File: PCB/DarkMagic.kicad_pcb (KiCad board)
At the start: 6 copper layers, 157 x 73 mm, 212 parts, among them IC1 5PB1106PGGI8, IC10 MMBT3904-AQ, IC11 MMBT3904-AQ, IC12 SN74LVC1G125DBVT, IC13 SN74LVC1G125DBVT, IC14 LM3940IMP-3.3_NOPB, IC15 SN74LVC1G125DBVT, IC17 LM393DR, IC2 ESP32-WROOM-32UE-N16, IC3 MMBT3904-AQ, IC4 MMBT3904-AQ, IC5 W5500, IC6 CP2102N-A02-GQFN24, IC7 USBLC6-2SC6, IC8 LMR33640ADDAR, J1 USB_C_Receptacle_USB2.0_16P, J2 TMJ0026ABNL, J3 5747842-2, J4 Screw_Terminal_01x02, J5 Screw_Terminal_01x02, J6 5747842-2, J7 171825-2, J9 Conn_01x04, Q1 SQ2319ADS-T1_BE3, Q2 SQ2348ES-T1_BE3, U1 SC16IS752IPW_128, U2 SC16IS752IPW_128, U3 CD74HC138QM96Q1, U4 SC16IS752IPW_128, U5 SC16IS752IPW_128, U6 SC16IS752IPW_128, U7 SC16IS752IPW_128, Y2 ASE-14.7456MHZ-LC-T, Y3 ASE-25.000MHZ-LC-T

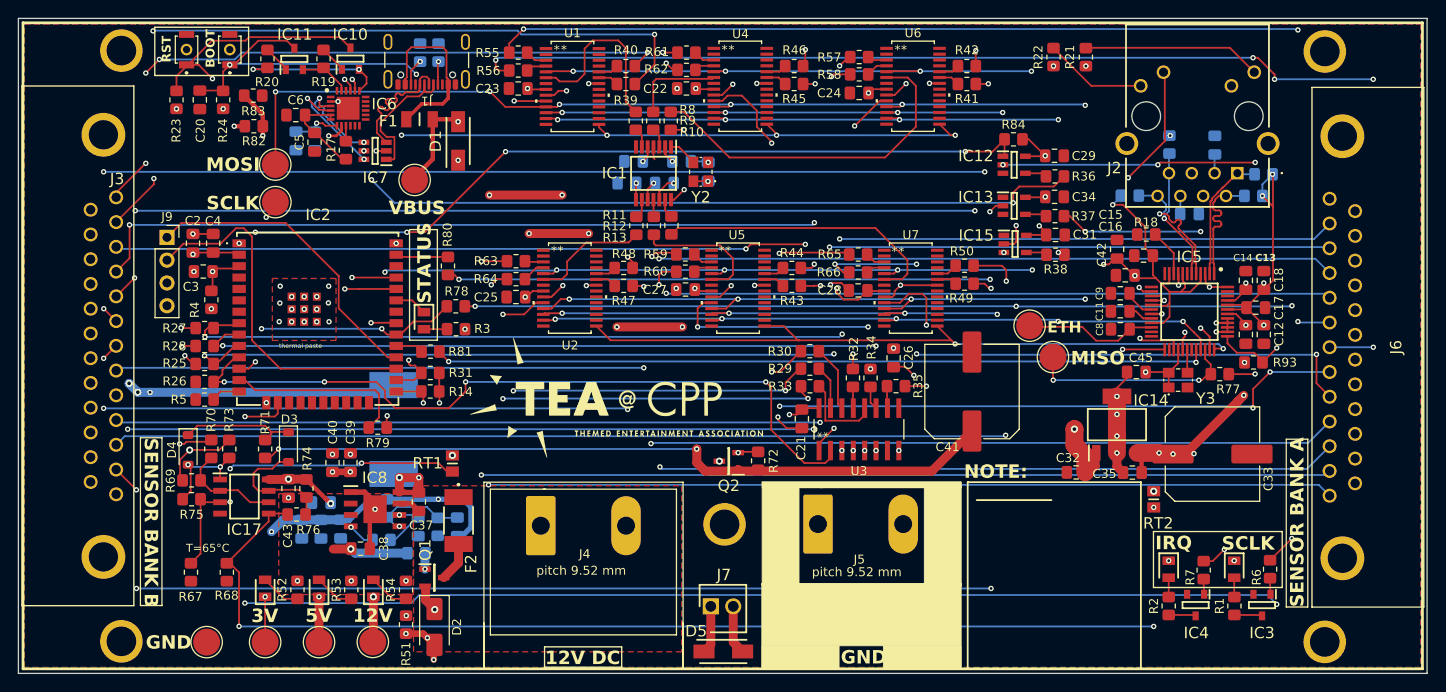
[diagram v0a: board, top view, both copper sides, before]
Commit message: Diagnosing Ethernet Controller
The Ethernet chip is dead, we'll need a new one. Minor optimizations everywhere.
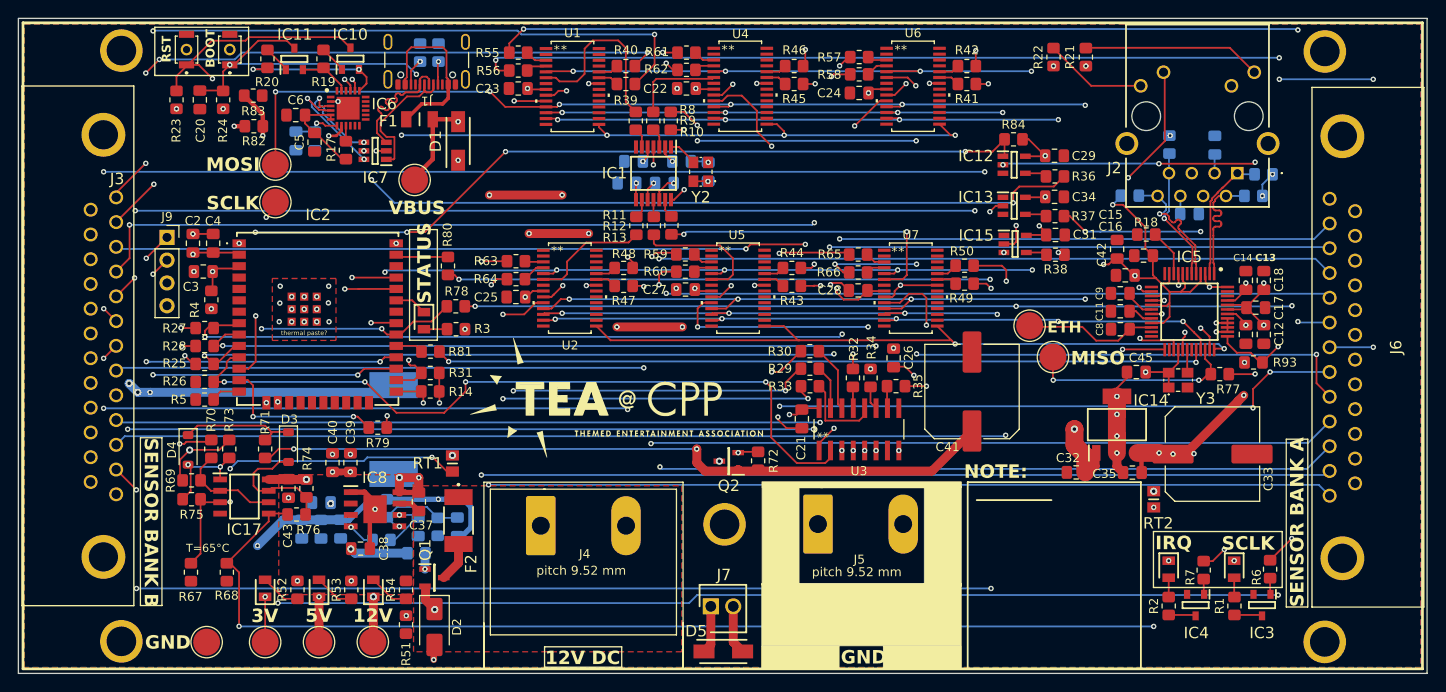
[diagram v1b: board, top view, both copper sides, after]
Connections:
- IC2 pad 23: /IO15 -> unconnected-(IC2-IO15-Pad23)
- J9 pad 3: GND -> +3V3
- J9 pad 4: +3V3 -> GND
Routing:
- net +3V3: track 232.0 -> 217.5 mm
- net /12VIN: track 225.2 -> 216.0 mm
- net /IO17: track 34.5 -> 42.9 mm, vias 0 -> 3
- net /W5500_RST: track 177.4 -> 170.0 mm
- net GND: track 89.7 -> 86.7 mm, vias 72 -> 70
- net +5V: track 304.0 -> 306.2 mm
- net /ESP_USRSTT: track 20.5 -> 18.7 mm, vias 0 -> 2
- net /XS6: track 32.2 -> 33.9 mm, vias 0 -> 2
- net /ESP_IRQ: track 225.6 -> 226.8 mm
- net /RXA1D: track 136.4 -> 137.5 mm
- net /IO16: track 40.3 -> 40.8 mm, vias 0 -> 3
- net /ESP_A1: track 82.6 -> 83.1 mm
- net /XS3: track 39.1 -> 39.5 mm, vias 0 -> 4
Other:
- board text added: "thermal paste?"
- board text removed: "thermal paste"
